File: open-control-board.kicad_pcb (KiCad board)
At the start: 4 copper layers, 69 x 110 mm, 144 parts, among them CN1 Service boiler fill sensor, CN10 LCC Port, CN2 Water tank level switch, CN3 NTC Service Boiler, CN4 NTC Brew Boiler, CN5 Service boiler relay, CN6 Conn_02x04_Counter_Clockwise, CN7 Brew Switch, CN8 12V Separate Supply, CN9 Brew boiler relay, J1 USB_B_Micro, J10 Conn_01x04_Pin, J11 Conn_01x04_Pin, J12 Conn_02x06_Odd_Even, J13 Conn_02x05_Odd_Even, J14 Conn_02x04_Odd_Even, J15 Conn_02x05_Odd_Even, J16 USB_B_Micro, J17 BM04B-SRSS-TB(LF)(SN), J18 Conn_01x03_Pin, J2 BM04B-SRSS-TB(LF)(SN), J3 TE 160650-2, J4 TE 160650-2, J5 TE 160650-2, J6 TE 160650-2, J7 TE 160650-2, J8 TE 160650-2, K1 RT314A12, Q1 AO3401A, Q11 DMN63D8LDW, Q2 AO3401A, Q3 Q_PMOS-E_DUAL_Generic_SEP_S1G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, Q4 DMN63D8LDW, Q5 Q_PMOS-E_DUAL_Generic_SEP_S1G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, Q6 DMN63D8LDW, SW1 SW_Push, SW2 SW_Push, SW3 SW_Push, SW4 SW_Push, U1 TPS82130, U10 FDC1004, U11 ALDP112, U12 ALDP112, U13 ALDP112, U15 STPIC6C595TTR, U16 STPIC6C595TTR, U3 TPS82130, U4 RP2040, U5 ESP32-S3-WROOM-1, U7 TXB0108PWR, U8 ADS1115IDGS, U9 W25Q16JVUXIQ, Y1 XYDBPCNANF-12MHZ

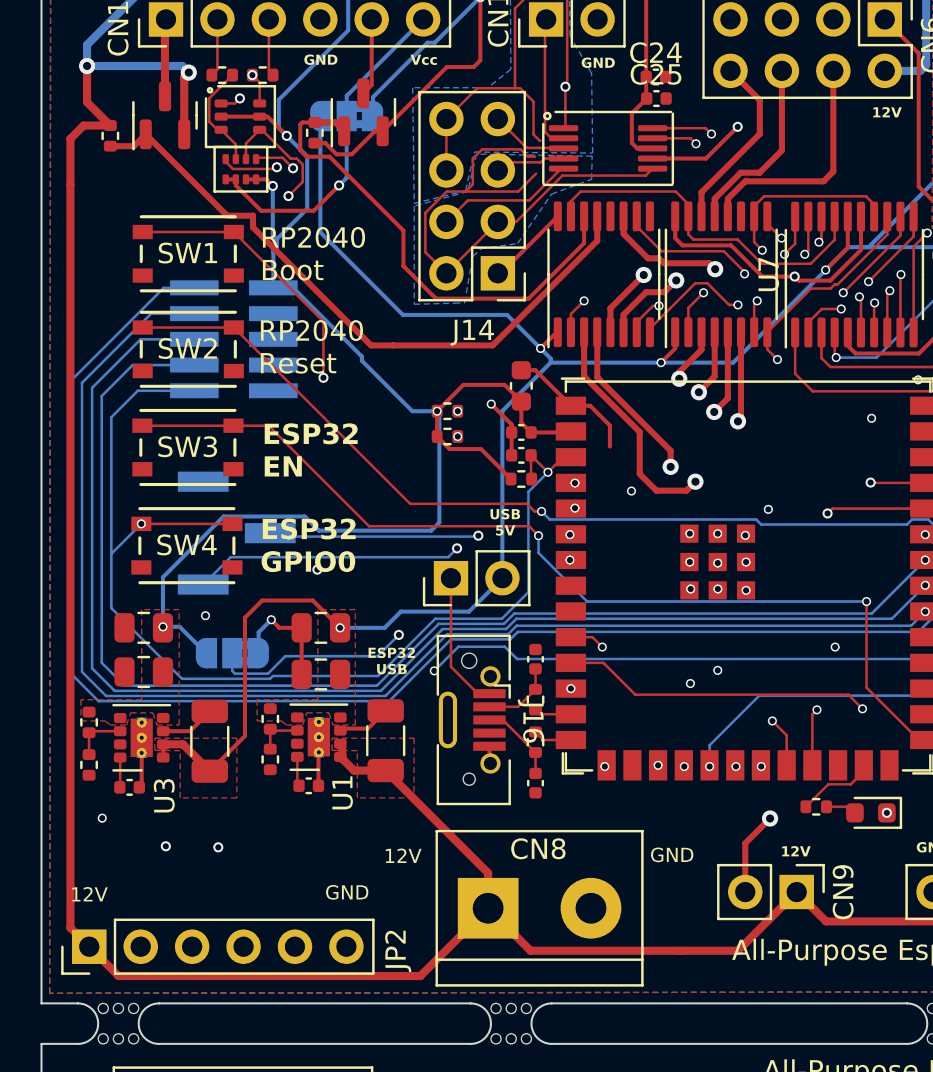
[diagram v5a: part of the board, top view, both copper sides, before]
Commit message: Cheaper resistors
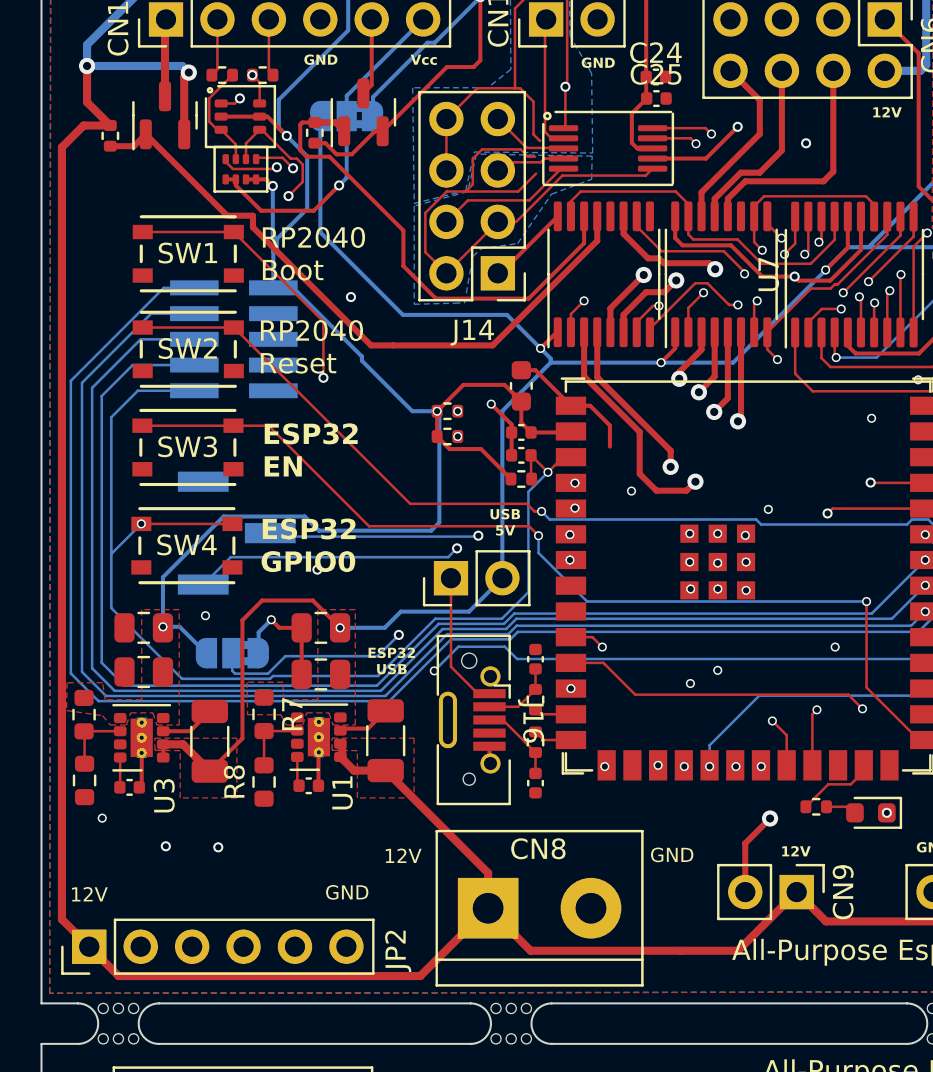
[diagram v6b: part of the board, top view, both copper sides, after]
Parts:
- C1, C5: value 5.6 nF, 50V -> 6.8 nF, 50V
- R10: value 10K -> 24K; footprint Resistor_SMD:R_0402_1005Metric -> Resistor_SMD:R_0603_1608Metric
- R7: value 53K6 -> 430K; footprint Resistor_SMD:R_0402_1005Metric -> Resistor_SMD:R_0603_1608Metric
- R8: value 10K -> 82K; footprint Resistor_SMD:R_0402_1005Metric -> Resistor_SMD:R_0603_1608Metric
- R9: value 31K6 -> 75K; footprint Resistor_SMD:R_0402_1005Metric -> Resistor_SMD:R_0603_1608Metric
- moved R8 1.16 mm to (63.0, 67.6)
- moved R10 0.80 mm to (54.1, 67.5)
- moved R9 0.46 mm to (54.1, 64.2)
- moved R7 0.38 mm to (63.0, 64.2)
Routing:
- net Net-(U1-FB): track 2.34 -> 3.35 mm
- net Net-(U3-FB): track 2.65 -> 3.51 mm
- net GND: vias 38 -> 40

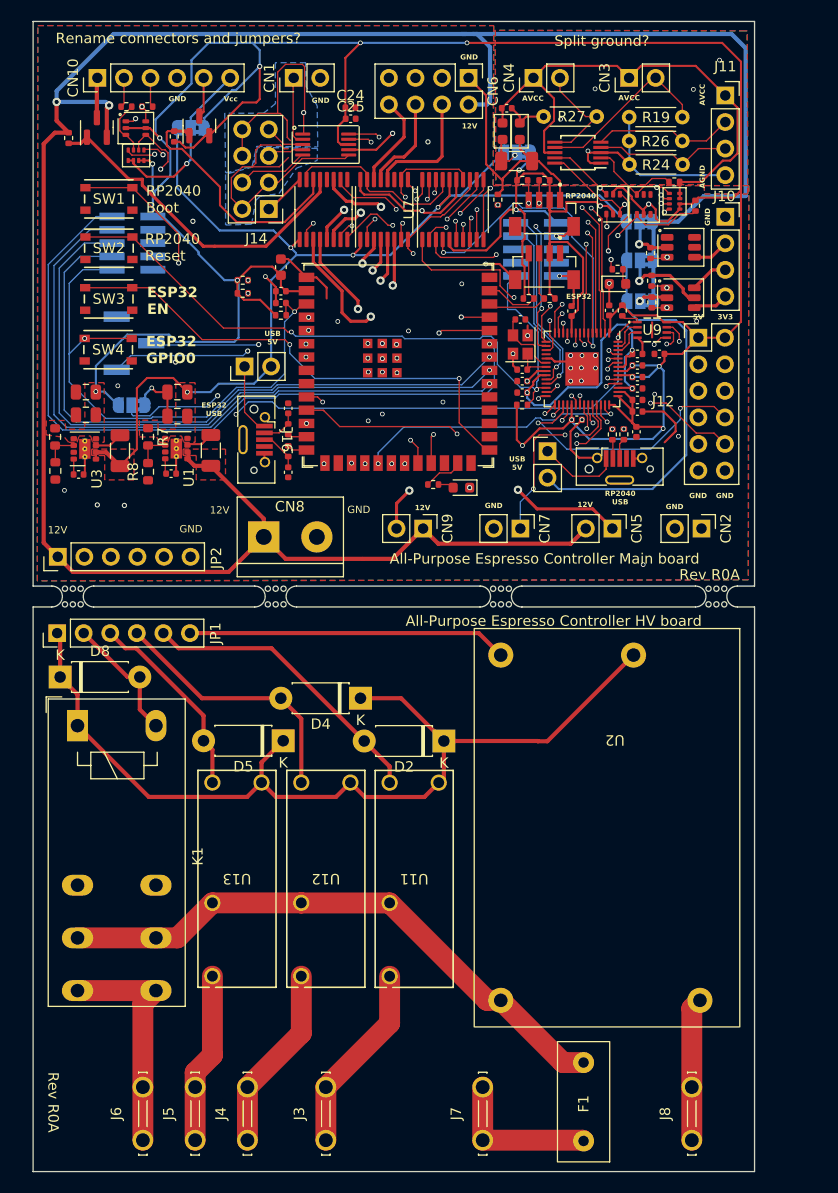
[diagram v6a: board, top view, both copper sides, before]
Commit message: Split HV board into separate project
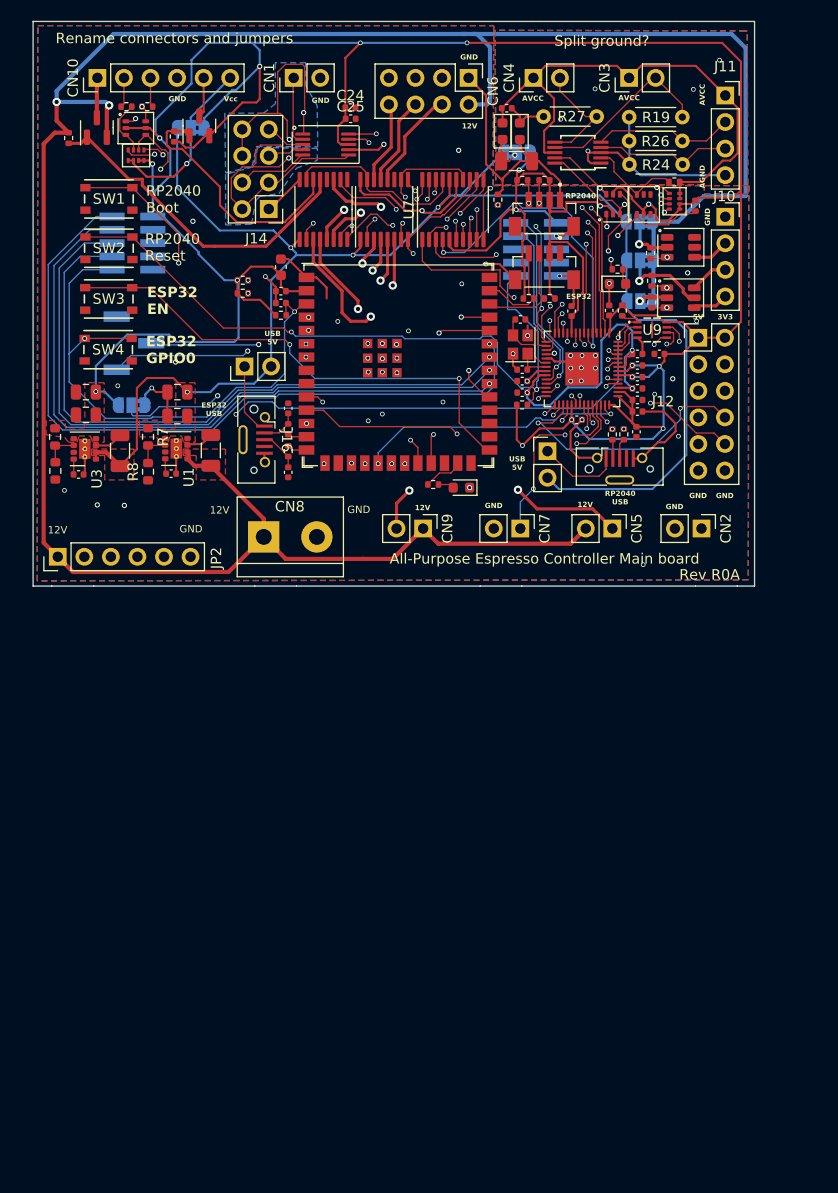
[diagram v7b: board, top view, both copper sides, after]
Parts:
- removed D2, D4, D5, D8: 1N4001, Diode_THT:D_DO-41_SOD81_P7.62mm_Horizontal
- removed F1: Schurter FRT 250T 7100.1009.13, 1289:FRT 250T
- removed J3, J4, J5, J6, J7, J8: TE 160650-2, 1289:KEYSTONE_1289
- removed JP1: Conn_01x06_Pin, Connector_PinHeader_2.54mm:PinHeader_1x06_P2.54mm_Vertical
- removed K1: RT314A12, Relay_THT:Relay_SPDT_Schrack-RT1-16A-FormC_RM5mm
- removed U11, U12, U13: ALDP112, ALDP112:PAN_ALD_PAN
- removed U2: ~, ECE05:ECE10
- removed locked, mouse-bite-2mm-slot (x3): VAL**, Panelization:mouse-bite-2mm-slot
- turned JP13 to 0 degrees
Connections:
- JP13 pad 1: +3V3 -> +5V
- JP13 pad 3: +5V -> +3V3
- U5 pad 31: unconnected-(U5-GPIO38/FSPIWP/SUBSPIWP-Pad31) -> GP15
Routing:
- net +12VA: track 90.2 -> 0.00 mm
- net PH: track 56.1 -> 0.00 mm
- net GND1: track 30.6 -> 0.00 mm
- net FA7_CTRL: track 28.5 -> 0.00 mm
- net FA8_CTRL: track 25.2 -> 0.00 mm
- net Net-(J6-Pin_1): track 22.3 -> 0.00 mm
- net FA9_CTRL: track 18.9 -> 0.00 mm
- net Net-(J3-Pin_1): track 18.2 -> 0.00 mm
- net Net-(J4-Pin_1): track 17.8 -> 0.00 mm
- net Net-(J5-Pin_1): track 16.4 -> 0.00 mm
- net GP15: track 0.00 -> 15.0 mm, vias 0 -> 2
- net PH_PRE_FUSE: track 14.8 -> 0.00 mm
- net N: track 13.7 -> 0.00 mm
- net FA10_CTRL: track 12.4 -> 0.00 mm
- net CN6_4: track 11.6 -> 9.64 mm
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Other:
- board size 69 x 110 mm -> 69 x 54 mm
- board text added: "Rename connectors and jumpers"
- board text removed: "All-Purpose Espresso Controller HV board"
- board text removed: "Height: <16 mm over board"
- board text removed: "Rename connectors and jumpers?"
